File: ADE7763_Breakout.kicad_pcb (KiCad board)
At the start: 2 copper layers, 32.7 x 26.7 mm, 32 parts, among them J1 10p-2.54, Q1 3.58MHz, U1 ADE7763ARSZSSOP20

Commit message: Bump version number
Signed-off-by: Tisham Dhar <whatnickd@gmail.com>
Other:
- board text added: "v4.0 11/02/2020"
- board text removed: "v1.0 25/11/2015"
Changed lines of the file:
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@@
     (effects (font (size 0.77216 0.77216) (thickness 0.16256)) (justify left bottom mirror))
   )
-  (gr_text "v1.0 25/11/2015" (at 152.5777 97.785) (layer B.SilkS)
+  (gr_text "v4.0 11/02/2020" (at 152.5777 97.785) (layer B.SilkS)
     (effects (font (size 0.77216 0.77216) (thickness 0.16256)) (justify left bottom mirror))
   )

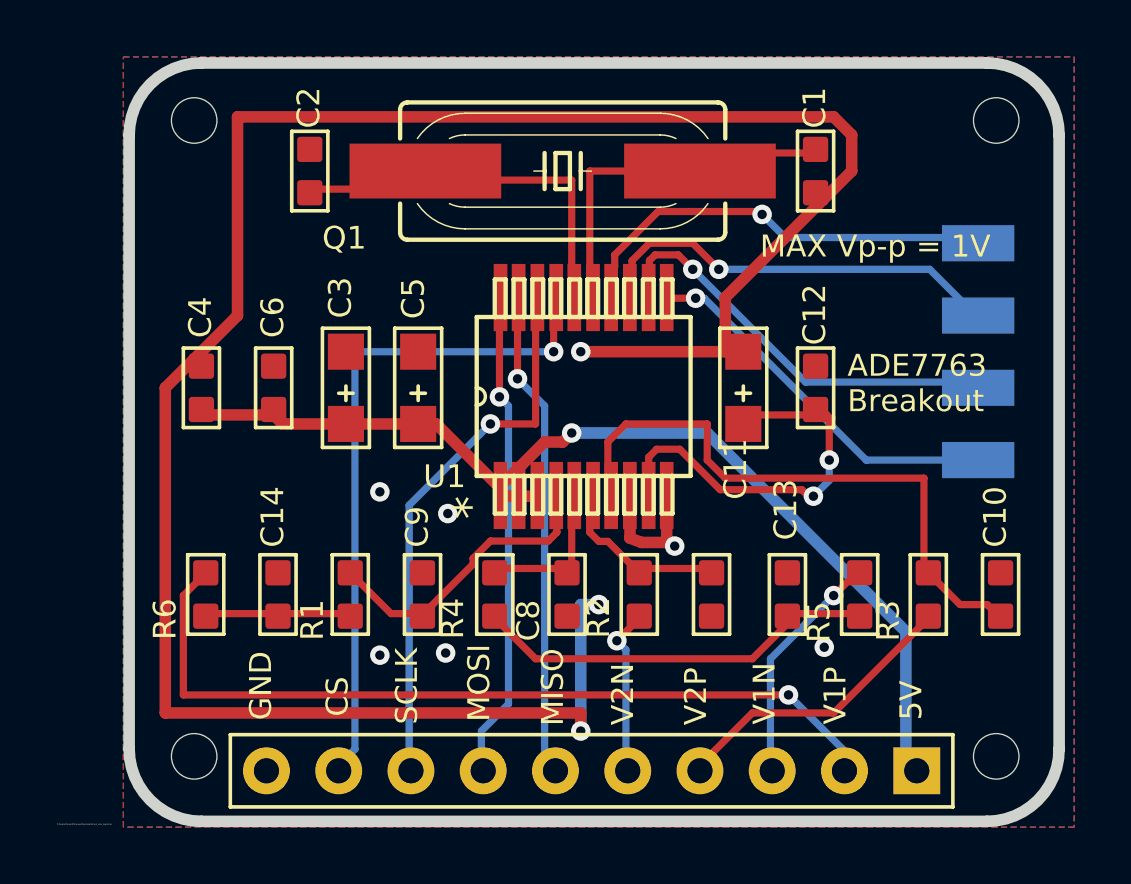
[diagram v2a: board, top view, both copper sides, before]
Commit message: Prevent bridging across SMD pins
Signed-off-by: Tisham Dhar <whatnickd@gmail.com>
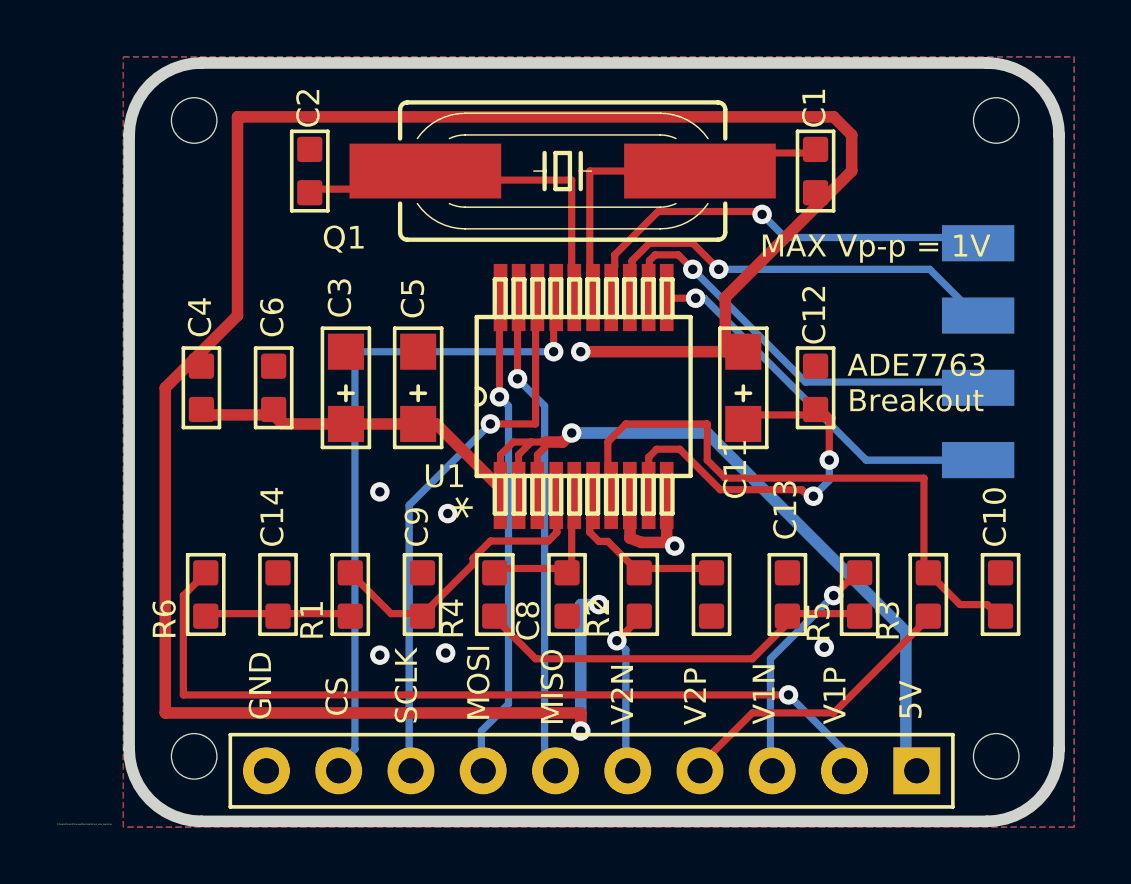
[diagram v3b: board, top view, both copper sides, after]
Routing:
- net 5V: track 36.6 -> 40.3 mm
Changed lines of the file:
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@@
     (thickness 1.6)
     (drawings 34)
-    (tracks 232)
+    (tracks 238)
     (zones 0)
     (modules 32)
@@
   (via (at 143.2813 112.4154) (size 0.6858) (drill 0.3302) (layers Top Bottom) (net 8))
   (via (at 156.5909 112.2122) (size 0.6858) (drill 0.3302) (layers Top Bottom) (net 8))
-  (segment (start 145.8086 106.9036) (end 145.1736 106.9036) (width 0.4064) (layer Top) (net 9))
   (segment (start 145.1736 106.9036) (end 145.2117 106.8782) (width 0.4064) (layer Top) (net 9))
-  (segment (start 145.8086 106.9036) (end 146.4436 106.9036) (width 0.4064) (layer Top) (net 9))
   (segment (start 146.4436 106.9036) (end 146.5071 106.8782) (width 0.4064) (layer Top) (net 9))
   (segment (start 145.8086 106.9036) (end 145.8467 106.8782) (width 0.4064) (layer Top) (net 9))
@@
   (segment (start 147.3961 104.9986) (end 147.7136 104.6811) (width 0.4064) (layer Top) (net 9))
   (segment (start 146.7611 104.9986) (end 147.3961 104.9986) (width 0.4064) (layer Top) (net 9))
-  (segment (start 145.1736 106.5861) (end 146.7611 104.9986) (width 0.4064) (layer Top) (net 9))
   (segment (start 159.7786 116.4286) (end 159.8421 116.5556) (width 0.4064) (layer Bottom) (net 9))
   (segment (start 145.1736 106.5861) (end 145.2117 106.8782) (width 0.4064) (layer Top) (net 9))
   (via (at 147.7136 104.6811) (size 0.6858) (drill 0.3302) (layers Top Bottom) (net 9))
+  (segment (start 146.7611 105.1931) (end 146.7611 104.9986) (width 0.25) (layer Top) (net 9))
+  (segment (start 146.5071 105.4471) (end 146.7611 105.1931) (width 0.25) (layer Top) (net 9))
+  (segment (start 146.5071 106.8782) (end 146.5071 105.4471) (width 0.25) (layer Top) (net 9))
+  (segment (start 145.8467 105.4471) (end 145.8467 106.8782) (width 0.25) (layer Top) (net 9))
+  (segment (start 146.2952 104.9986) (end 145.8467 105.4471) (width 0.25) (layer Top) (net 9))
+  (segment (start 146.7611 104.9986) (end 146.2952 104.9986) (width 0.25) (layer Top) (net 9))
+  (segment (start 145.2117 105.4471) (end 145.2117 106.8782) (width 0.25) (layer Top) (net 9))
+  (segment (start 145.6602 104.9986) (end 145.2117 105.4471) (width 0.25) (layer Top) (net 9))
+  (segment (start 146.2952 104.9986) (end 145.6602 104.9986) (width 0.25) (layer Top) (net 9))
   (segment (start 146.4436 112.6186) (end 145.1736 111.3486) (width 0.254) (layer Top) (net 10))
   (segment (start 154.0636 112.6186) (end 146.4436 112.6186) (width 0.254) (layer Top) (net 10))

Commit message: Start updating to sync with kicad better
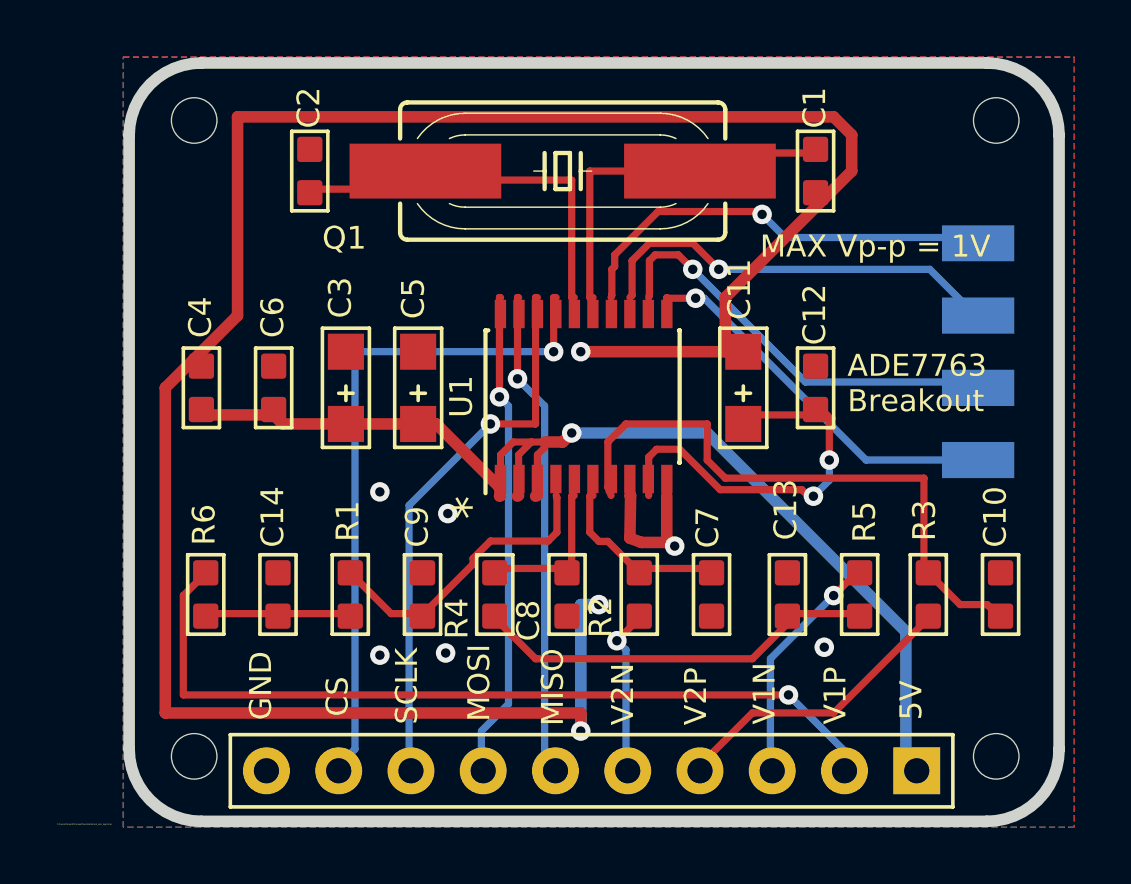
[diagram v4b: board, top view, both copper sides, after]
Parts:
- U1: footprint RS_20-M -> Package_SO:SSOP-20_4.4x6.5mm_P0.65mm
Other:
- net class Default removed

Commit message: Fix PCB for footprint and DRC
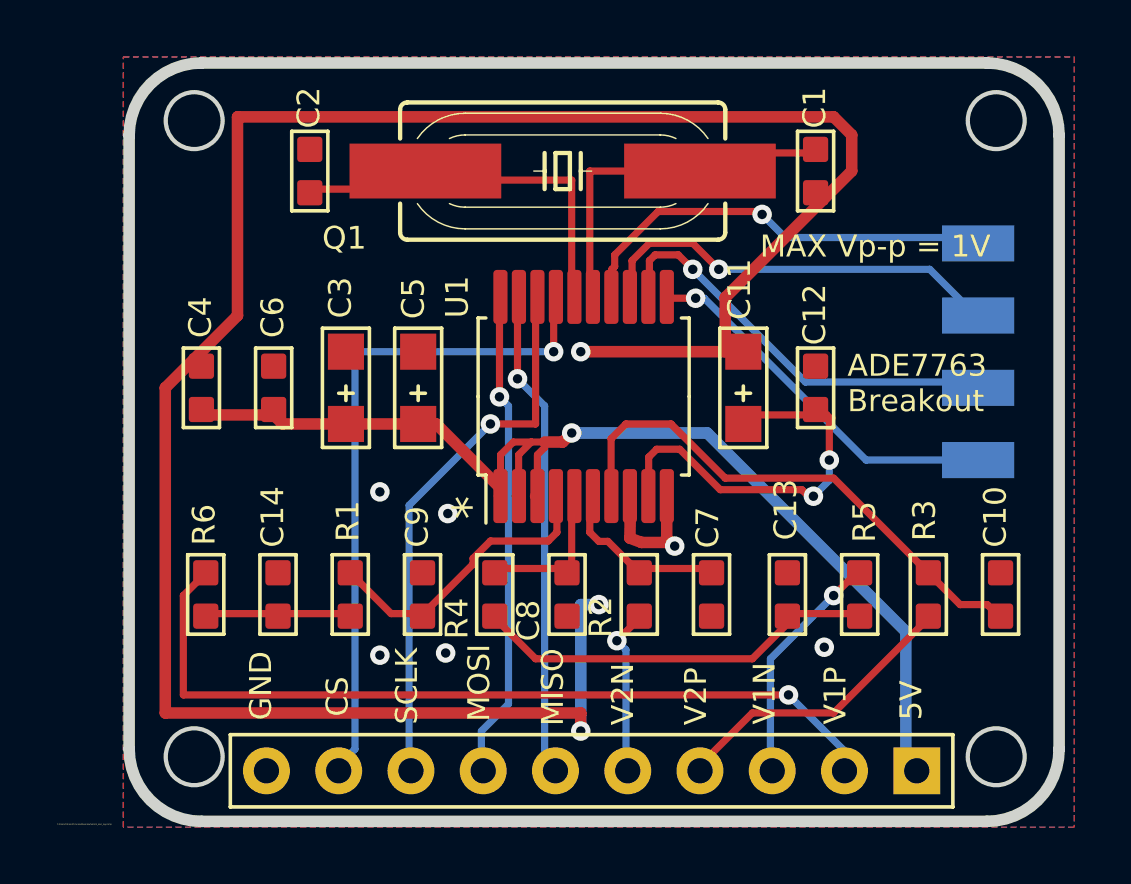
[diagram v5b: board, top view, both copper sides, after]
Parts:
- removed @HOLE0, @HOLE1, @HOLE2, @HOLE3: , 
- U1: footprint Package_SO:SSOP-20_4.4x6.5mm_P0.65mm -> Package_SO:SSOP-20_5.3x7.2mm_P0.65mm
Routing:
- net N$6: track 21.4 -> 18.7 mm
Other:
- outline, holes or cut-outs redrawn
